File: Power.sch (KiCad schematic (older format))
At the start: 33 parts, among them IC2 TPS73633, IC3 MCP73831/2-OT, IC4 TPS73618, IC5 MCP1640-SOT, IC6 TPS73633, J18 power switch, J7 Battery, Q1 Q_PMOS_GSD, SW2 Charge select

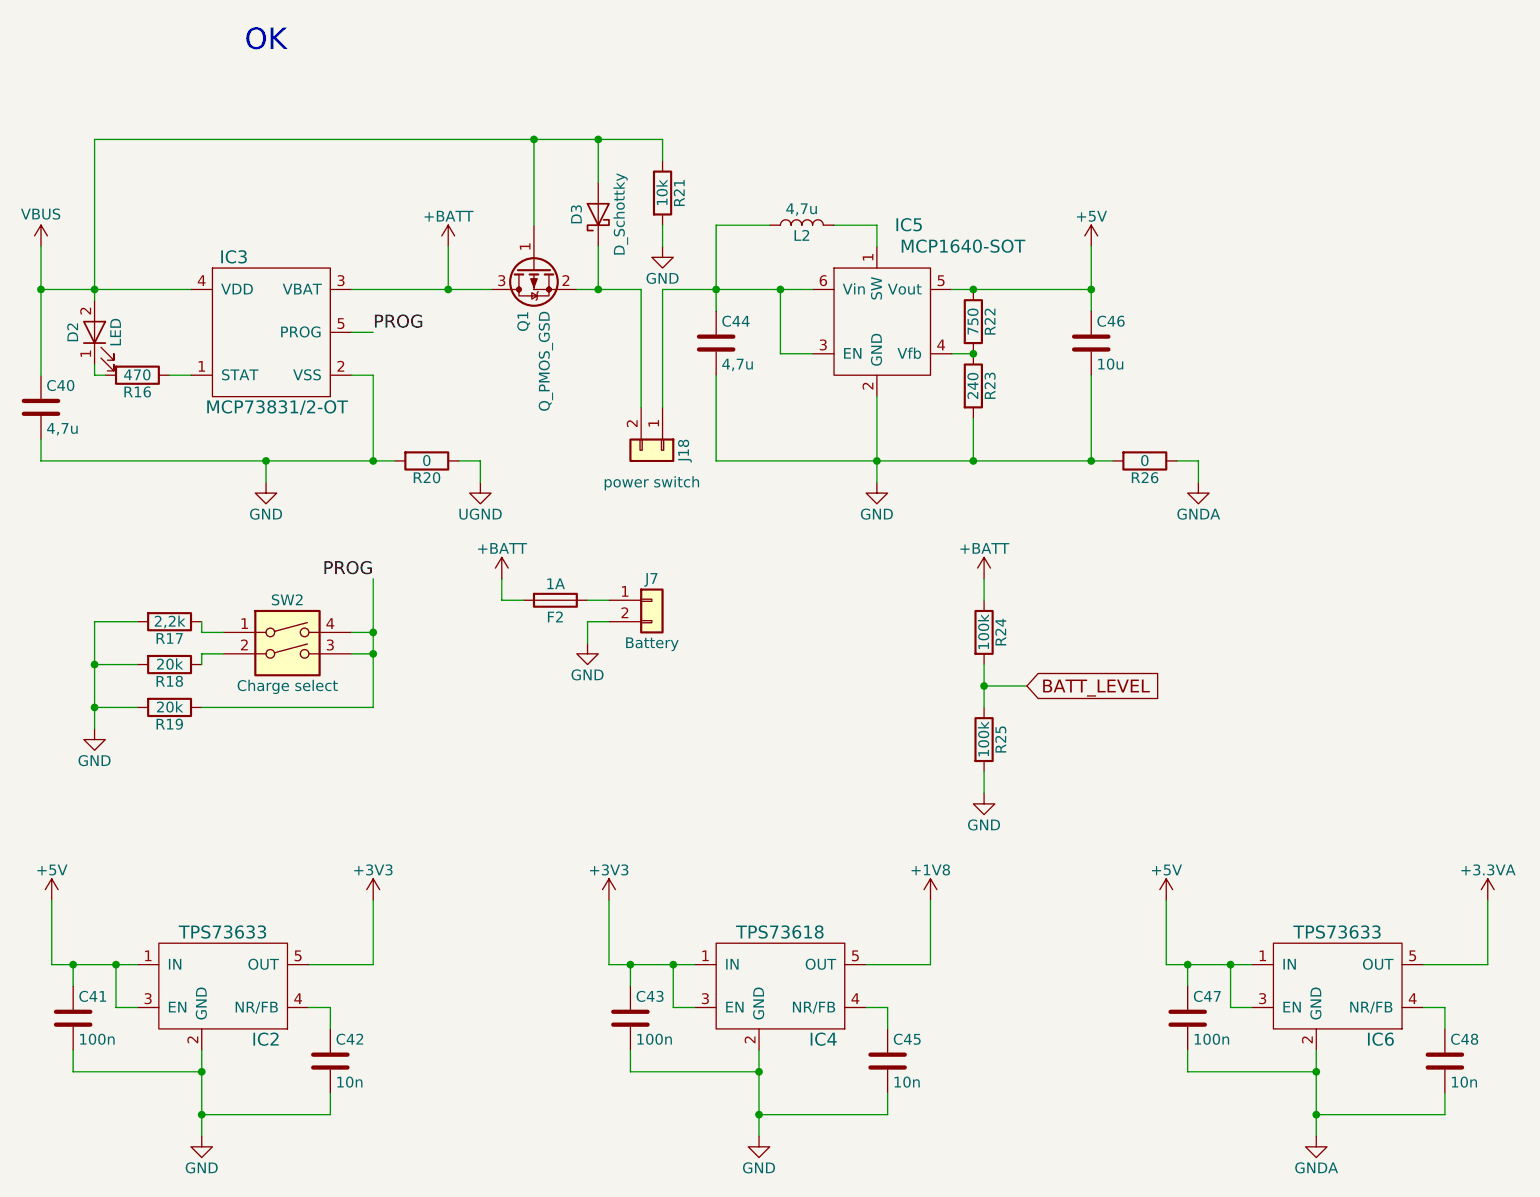
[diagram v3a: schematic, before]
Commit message: v0.2 ready for fabrication. Voltage regulators replaced by cheaper ones.
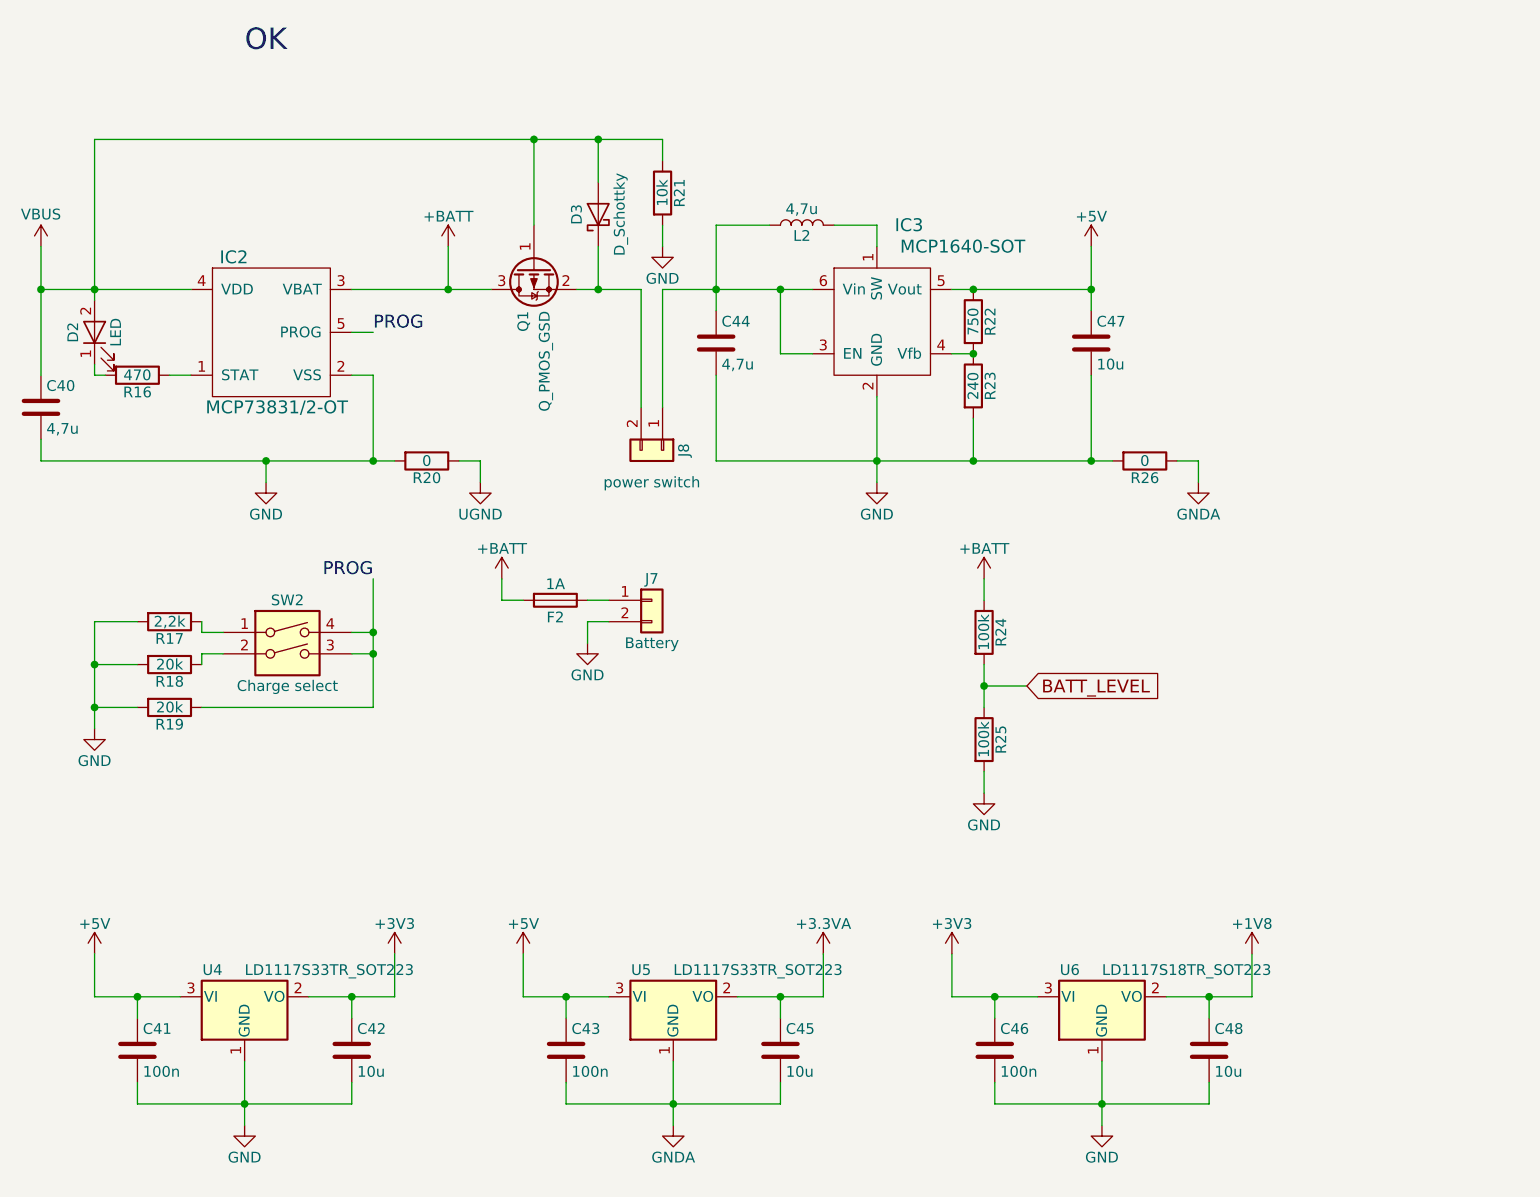
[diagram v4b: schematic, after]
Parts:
- removed C47: 100n, Capacitors_SMD:C_0603, symbol C
- removed IC2, IC6: TPS73633, TO_SOT_Packages_SMD:SOT-23-5, symbol TPS736xx
- removed IC4: TPS73618, TO_SOT_Packages_SMD:SOT-23-5, symbol TPS736xx
- added C46: 100n, Capacitors_SMD:C_0603, symbol C
- added U4, U5: LD1117S33TR_SOT223, TO_SOT_Packages_SMD:SOT-223-3_TabPin2, symbol LD1117S33TR_SOT223
- added U6: LD1117S18TR_SOT223, TO_SOT_Packages_SMD:SOT-223-3_TabPin2, symbol LD1117S18TR_SOT223
- C42, C45, C48: value 10n -> 10u
- renumbered C46 to C47, IC3 to IC2, IC5 to IC3, J18 to J8
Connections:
- net +1V8: now also C48.1, U6.2 (VO)
- net +3.3VA: now also C45.1, U5.2 (VO)
- net +3V3: now also C42.1, C46.1, U4.2 (VO), U6.3 (VI); no longer C43.1
- net +5V: now also C43.1, U4.3 (VI), U5.3 (VI)
- net GND: now also C48.2, C46.2, U4.1 (GND), U6.1 (GND); no longer C43.2, C45.2
- net GNDA: now also C43.2, C45.2, U5.1 (GND); no longer C48.2
